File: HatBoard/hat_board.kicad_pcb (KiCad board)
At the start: 4 copper layers, 88 x 94.5 mm, 52 parts, among them J2 Conn_01x04, J3 Z-DF11 FC Connection, J4 DF11 FC Connection, J5 DF11 FC Connection, J6 DF11 FC Connection, U10 VEML7700, U12 DRV2605LDGS, U13 TCA4311A, U17 TCA4311A, U21 TCA4311A, U27 TMP112AIDRLR, U4 TCA4311A, U5 TCA4311A, U9 TCA4311A

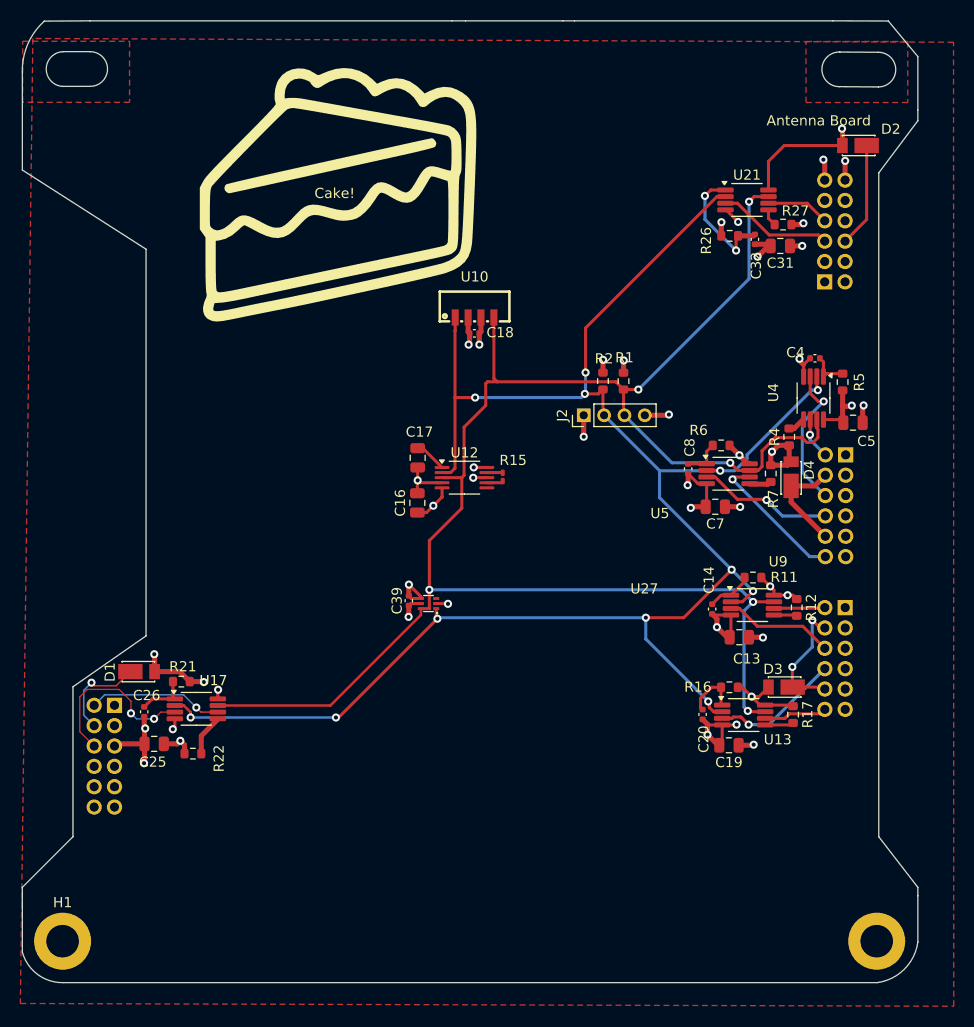
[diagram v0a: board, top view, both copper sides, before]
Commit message: added labels
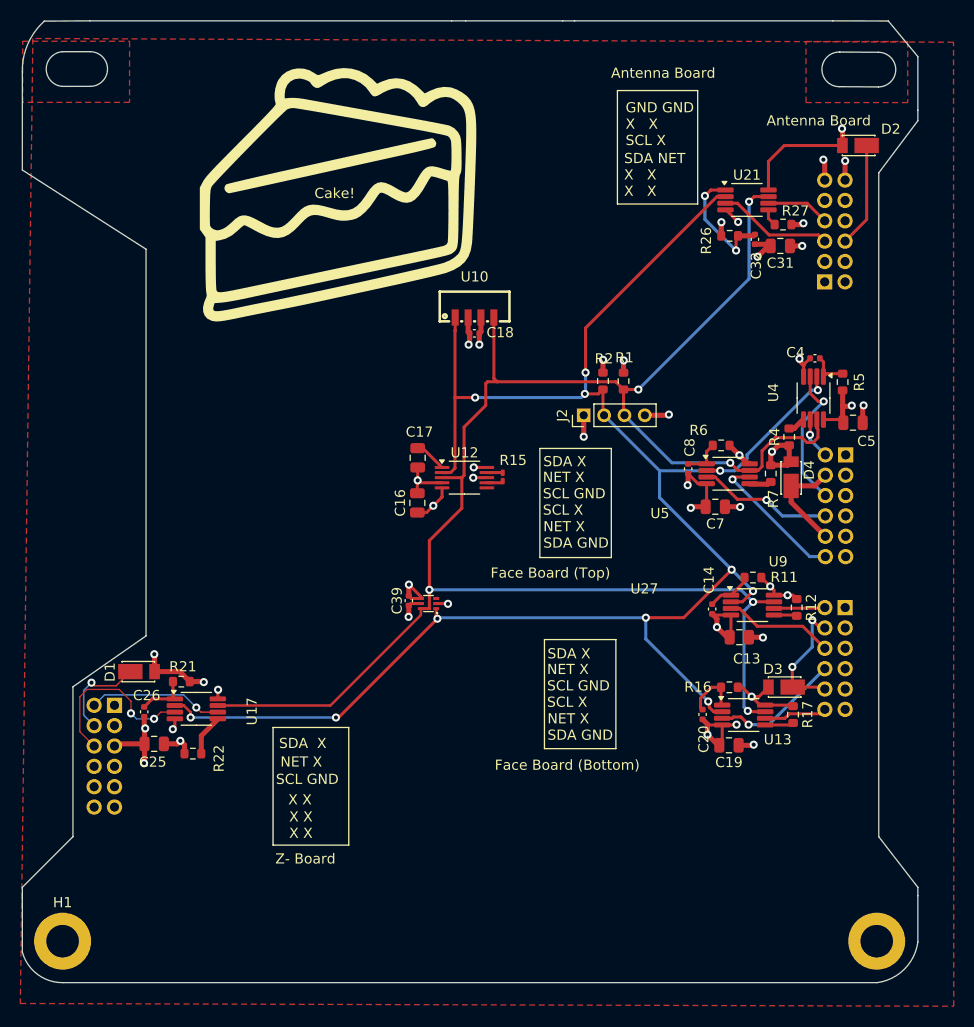
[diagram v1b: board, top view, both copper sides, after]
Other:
- board text added: "Face Board (Bottom)"
- board text added: "Face Board (Top)"
- board text added: "GND GND X X SCL X"
- board text added: "NET X"
- board text added: "NET X SCL GND SCL X"
- board text added: "NET X SDA GND"
- board text added: "SCL GND"
- board text added: "SDA NET X X X X"
- board text added: "SDA X"
- board text added: "X X"
- board text added: "X X X X"
- board text added: "Z- Board"

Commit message: new resiotr
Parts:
- removed H1, H2: MountingHole, MountingHole:MountingHole_3.2mm_M3_DIN965_Pad
- J3: value Z-DF11 FC Connection -> DF11 FC Connection
